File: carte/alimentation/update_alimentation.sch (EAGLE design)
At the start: 81 parts, among them IC1 LM2596T, IC2 LM2596T, IC4 DSPIC33FJ128MC804PT, J4 RJ11-2L-B, K2 RP811005, U2 LP2985-33DBVR, X10 22-23-2021, X11 22-23-2021, X9 22-23-2021

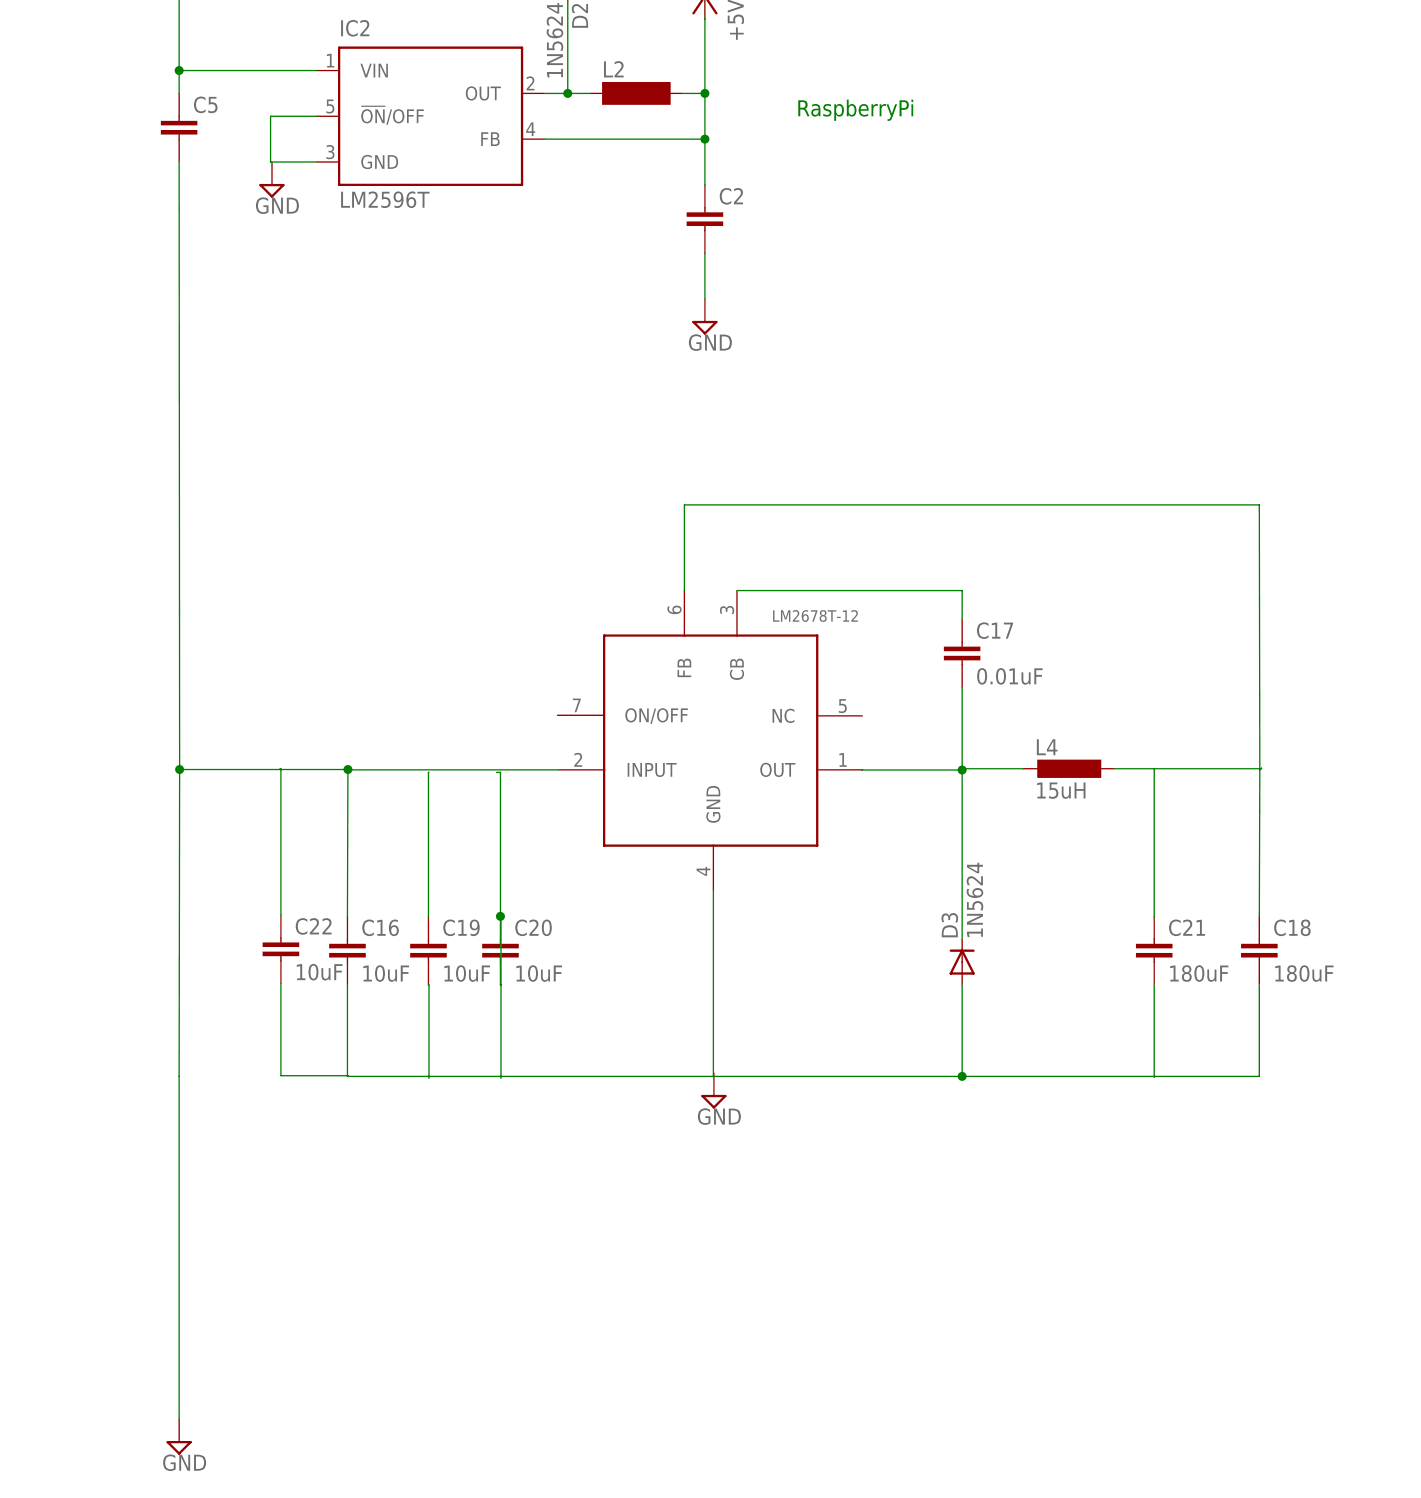
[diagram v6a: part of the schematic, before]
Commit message: LM2678S_ADJ dimmensionnement
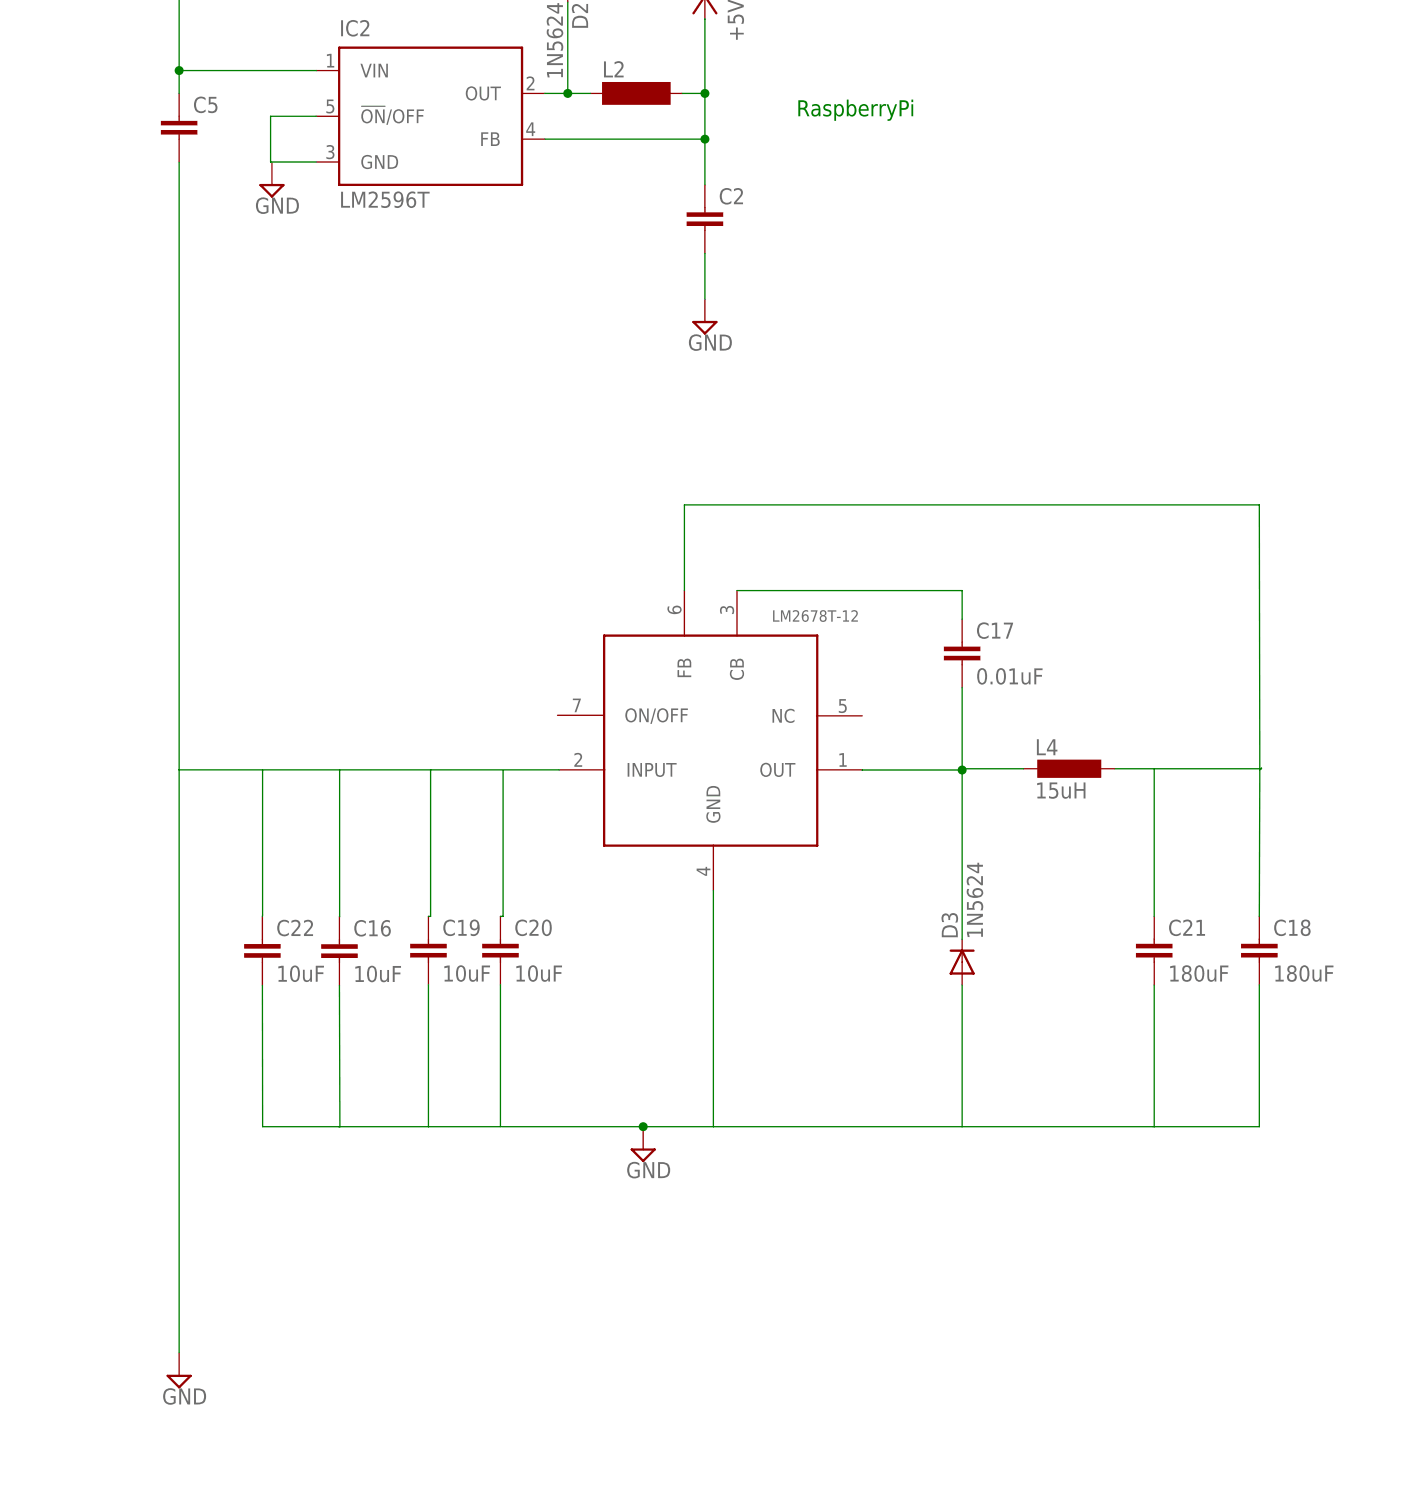
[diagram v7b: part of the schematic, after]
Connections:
- removed net N$25 (its old number): C22.2
- removed net N$29: C20.1, C20.2
- new net N$24: C16.1
- net GND: now also C18.2, C21.2, D3.A, LM2678T-12.GND; no longer C16.1
- net N$21: now also C16.2, C22.2; no longer C21.2
- net N$26: now also C19.2, C20.2; no longer C16.2, C18.2, D3.A, LM2678T-12.GND
- net N$28: now also C20.1; no longer C19.2
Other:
- moved on the sheet: C16, C22

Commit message: carte alim maj sch/brd
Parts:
- removed C3: 1000u, resistor:C-EUC0603
- removed D1, D2, D3: 1N5624, diode:1N5624
- removed K2: RP811005, relay:RP811005
- removed L1, L2: (no value), inductor-neosid:SM-L15A
- removed L4: 15uH, inductor-coilcraft:DO3316P
- removed LED2: (no value), eagle-ltspice:LED_E
- added C23, C24, C25: 100uF, rcl:C-EUC1210
- added C26, C30: 10uF, rcl:CPOL-EUD/7343-31W
- added C27: 220uF, rcl:CPOL-EUD/7343-31W
- added C28, C29: 68uF, rcl:CPOL-EUD/7343-31W
- added LED1: RED, led:LED5MM
- added LM2678S_ADJ: (no value), Robot_MT:LM2678
- added R7: 4.12k, resistor:R-EU_R0805
- added R8: 1k, resistor:R-EU_R0805
- added U$10, U$11: 53uH, Robot_MT:PE-54039NL
- added U$12: RJ26FX102, Robot_MT:RJ26FX102
- added U$2, U$3: (no value), Robot_MT:SCHOTTKY_TO220
- added U$4, U$5: (no value), Robot_MT:1N5820
- added U$6: T9GV1L14-5, Robot_MT:T9GV1L14-5
- added U$7: BSH108, Robot_MT:BSH108
- added U$8: 22.8uH, Robot_MT:P0841NL
- added U$9: 14.8uH, Robot_MT:P0846NL
- C1: value (none) -> 220uF; device resistor:C-EUC0603 -> rcl:CPOL-EUD/7343-31W; OC_FARNELL (none) -> 2283872
- C16, C19, C20: device resistor:C-EUC0603 -> rcl:CPOL-EUD/7343-31W; OC_FARNELL (none) -> 2424754
- C17: device resistor:C-EUC0603 -> rcl:C-EUC0603
- C18, C21: value 180uF -> 68uF; device resistor:C-EUC0603 -> rcl:CPOL-EUD/7343-31W; OC_FARNELL (none) -> 2524603
- C2, C4: value (none) -> 330uF; device resistor:C-EUC0603 -> rcl:CPOL-EUD/7343-31W; OC_FARNELL (none) -> 1135198
- C22: value 10uF -> 0.01uF; device resistor:C-EUC0603 -> rcl:C-EUC0603
- C5: value (none) -> 1000uF; device resistor:C-EUC0603 -> rcl:CPOL-EUE7.5-16
- R5: value 220 -> 500
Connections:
- removed net N$14 (its old number): C18.1, LM2678T-12.FB
- removed net N$20: C21.1
- removed net N$21: C16.2, C22.2
- removed net N$22: C22.1
- removed net N$23: IC2.!ON!/OFF, IC2.GND
- removed net N$24: C16.1
- removed net N$25: C19.1
- removed net N$26: C19.2, C20.2
- removed net N$27: IC1.!ON!/OFF, IC1.GND
- removed net N$28: C20.1
- removed net RB0: D5.A, K21.2
- removed net RB1: LED2.C, R5.1
- new net 5V_3A: X10-1.S, X11-1.S, X12-2.KL, X9-1.S
- new net N$15: C16.+, C19.+, C20.+, C26.+, C30.+, C4.+, C5.+, IC2.VIN, LM2678S_ADJ.INPUT, LM2678T-12.INPUT, R8.1, U$6G$2.P, X1-1.KL
- new net RA7: IC4.TCK/PMA7/RA7*, LED1.C, U$7.G
- new net RA8: IC4.TDO/PMA8/RA8*, R5.1
- new net V+: C18.+, C21.+, C28.+, C29.+, U$9.2
- net +5V: now also C1.+, D5.C, U$11.2, U$6G$1.1; no longer C2.1, L2.2
- net +5V_3A: now also C27.+, U$10.2; no longer C1.1, L1.2
- net GND: now also C1.-, C16.-, C18.-, C19.-, C2.-, C20.-, C21.-, C23.2, C24.2, C25.2, C26.-, C27.-, C28.-, C29.-, C30.-, C4.-, C5.-, IC1.!ON!/OFF, IC1.GND, IC2.!ON!/OFF, IC2.GND, LM2678S_ADJ.GND, U$2.A, U$3.A, U$4.A, U$5.A, U$7.S, X15-2.KL; no longer C1.2, C18.2, C2.2, C21.2, C3.1, C5.2, D1.A, D2.A, D3.A, LM2678T-12.INPUT
- net N$1: now also LED1.A, R5.2; no longer X13-1.KL
- net N$11: now also C17.2, LM2678T-12.OUT, U$3.C, U$9.1; no longer C4.1, IC1.VIN, X15-2.KL
- net N$12: now also U$10.1, U$4.C; no longer D1.C, L1.1
- net N$13: now also C22.1, LM2678S_ADJ.CB; no longer C3.2, C5.1, IC2.VIN, K22.O, X1-1.KL
- net N$16: now also C22.2, LM2678S_ADJ.OUT, U$2.C, U$8.1; no longer D5.C, K21.1
- net N$17: now also C23.1, C24.1, C25.1, U$12.E, U$8.2; no longer C17.2, D3.C, LM2678T-12.OUT
- net N$18: now also D5.A, U$6G$1.2, U$7.D; no longer L4.1
- net N$19: now also R7.2, U$12.S; no longer L4.2
- net N$6: now also C2.+, IC1.VIN, U$6G$2.S, X13-1.KL; no longer C4.2, K22.P
- net N$7: now also LM2678S_ADJ.FB, R7.1, R8.2; no longer LED2.A, R5.2
- net N$9: now also U$11.1, U$5.C; no longer D2.C, L2.1
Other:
- note removed: "Propulsion"
- note removed: "RaspberryPi"
- note removed: "dsPIC (gestion batterie)"
- moved on the sheet: C10, C11, C12, C13, C14, C15, C17, C22, C6, C7, C8, C9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
